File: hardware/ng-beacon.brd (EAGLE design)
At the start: 71.1 x 76.2 mm, 7 parts

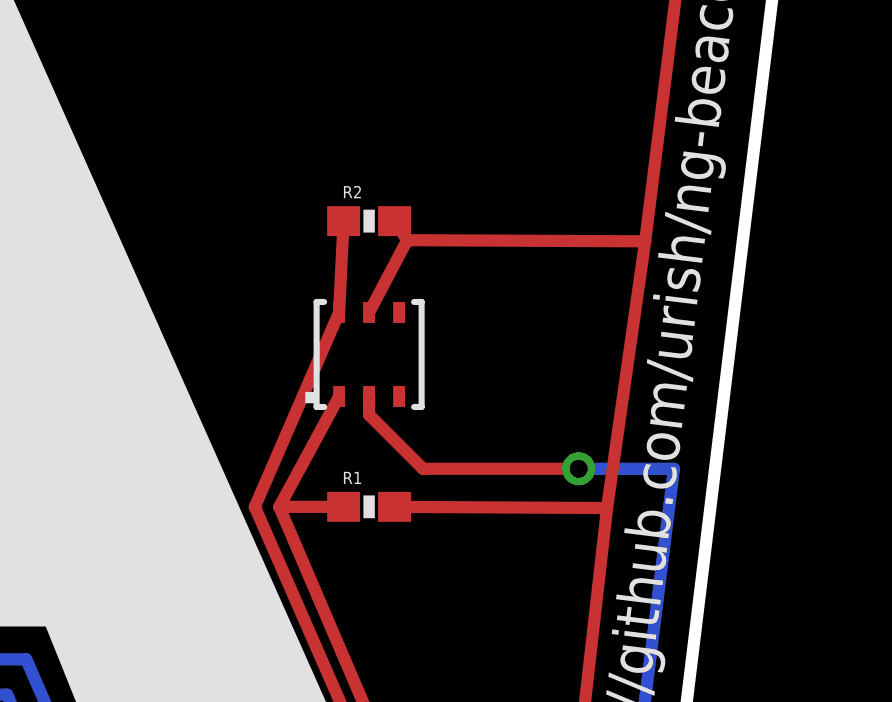
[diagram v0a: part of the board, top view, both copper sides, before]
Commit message: fix(pcb): remove I2C pullup resistors
it works fine without them, as the nRF51 has internal pullups
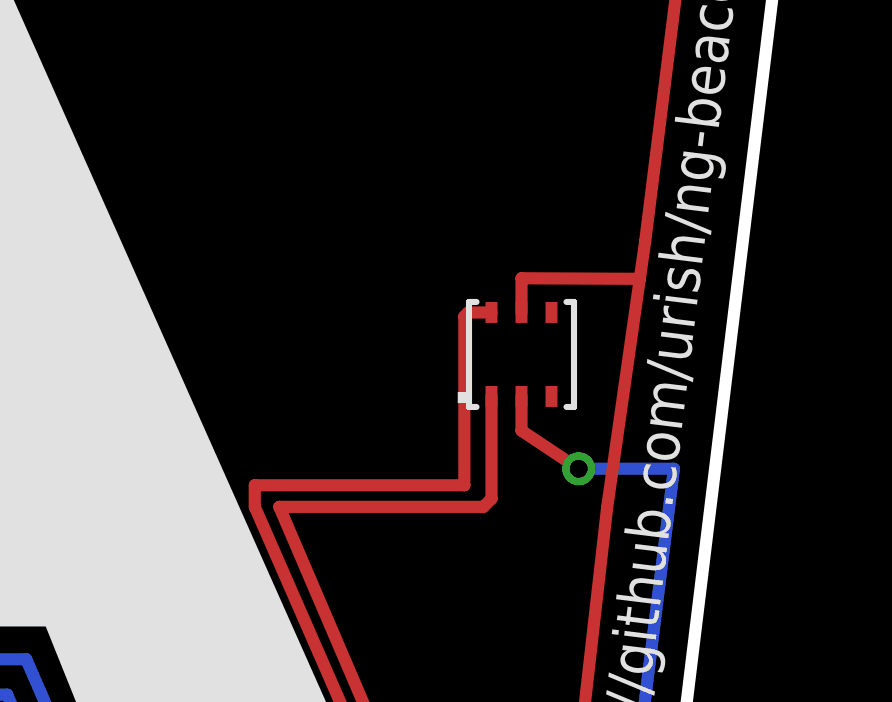
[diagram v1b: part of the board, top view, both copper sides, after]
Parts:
- removed R1, R2: 10K, SparkFun-Resistors:0603-RES
- moved SN1 5.08 mm to (71.1, 35.6)
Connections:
- net SCL: no longer R2.1
- net SDA: no longer R1.1
- net VIN: no longer R1.2, R2.2
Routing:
- net VIN: track 96.9 -> 83.5 mm
- net GND: track 130.4 -> 125.5 mm
- net SDA: track 34.6 -> 38.9 mm
- net SCL: track 35.8 -> 40.0 mm
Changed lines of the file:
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@@
 <attribute name="VALUE" x="64.3222" y="15.616859375" size="1.27" layer="27" rot="R209"/>
 </element>
-<element name="SN1" library="sensirion" package="DFN6/SHT" value="SHT21" x="66.04" y="35.56" smashed="yes">
-<attribute name="VALUE" x="68.915" y="33.685" size="0.8128" layer="27" ratio="10" rot="R90"/>
-</element>
-<element name="R1" library="SparkFun-Resistors" package="0603-RES" value="10K" x="66.04" y="30.48">
-<attribute name="PROD_ID" value="RES-00824" x="66.04" y="30.48" size="1.778" layer="27" display="off"/>
-</element>
-<element name="R2" library="SparkFun-Resistors" package="0603-RES" value="10K" x="66.04" y="40.005">
-<attribute name="PROD_ID" value="RES-00824" x="66.04" y="40.005" size="1.778" layer="27" display="off"/>
+<element name="SN1" library="sensirion" package="DFN6/SHT" value="SHT21" x="71.12" y="35.56" smashed="yes">
+<attribute name="VALUE" x="73.995" y="33.685" size="0.8128" layer="27" ratio="10" rot="R90"/>
 </element>
 </elements>
@@
 <contactref element="SN1" pad="2"/>
 <wire x1="52.07" y1="12.7" x2="58.02453125" y2="8.641059375" width="0.4064" layer="1"/>
-<wire x1="66.04" y1="34.16" x2="66.04" y2="33.54605" width="0.4064" layer="1"/>
-<wire x1="66.04" y1="33.54605" x2="67.83605" y2="31.75" width="0.4064" layer="1"/>
-<wire x1="67.83605" y1="31.75" x2="73.025" y2="31.75" width="0.4064" layer="1"/>
 <via x="73.025" y="31.75" extent="1-16" drill="0.6" shape="square"/>
 <wire x1="73.025" y1="31.75" x2="76.2" y2="31.75" width="0.4064" layer="16"/>
@@
 <wire x1="59.8045" y1="7.40863125" x2="58.600153125" y2="7.71598125" width="0.4064" layer="16"/>
 <wire x1="58.600153125" y1="7.71598125" x2="58.02453125" y2="8.641059375" width="0.4064" layer="16"/>
+<wire x1="73.025" y1="31.75" x2="71.12" y2="33.02" width="0.4064" layer="1"/>
+<wire x1="71.12" y1="33.02" x2="71.12" y2="34.16" width="0.4064" layer="1"/>
 </signal>
 <signal name="N$1">
@@
 <wire x1="69.215" y1="13.97" x2="72.39" y2="16.51" width="0.4064" layer="1"/>
 <wire x1="72.39" y1="16.51" x2="73.972615625" y2="30.440921875" width="0.4064" layer="1"/>
-<wire x1="73.972615625" y1="30.440921875" x2="75.242615625" y2="39.330921875" width="0.4064" layer="1"/>
+<wire x1="73.972615625" y1="30.440921875" x2="75.064034375" y2="38.080853125" width="0.4064" layer="1"/>
+<wire x1="75.064034375" y1="38.080853125" x2="75.242615625" y2="39.330921875" width="0.4064" layer="1"/>
 <wire x1="75.242615625" y1="39.330921875" x2="78.105" y2="62.23" width="0.4064" layer="1"/>
 <wire x1="78.105" y1="62.23" x2="73.9255625" y2="63.7972875" width="0.4064" layer="1"/>
 <wire x1="73.9255625" y1="63.7972875" x2="72.749771875" y2="63.21341875" width="0.4064" layer="1"/>
 <wire x1="72.749771875" y1="63.21341875" x2="72.597159375" y2="62.70240625" width="0.4064" layer="1"/>
-<wire x1="66.04" y1="36.96" x2="67.31" y2="39.37" width="0.4064" layer="1"/>
-<wire x1="67.31" y1="39.37" x2="75.242615625" y2="39.330921875" width="0.4064" layer="1"/>
-<contactref element="R1" pad="2"/>
-<contactref element="R2" pad="2"/>
-<wire x1="66.89" y1="30.48" x2="73.972615625" y2="30.440921875" width="0.4064" layer="1"/>
-<wire x1="66.89" y1="40.005" x2="67.31" y2="39.37" width="0.4064" layer="1"/>
+<wire x1="71.12" y1="36.96" x2="71.12" y2="38.1" width="0.4064" layer="1"/>
+<wire x1="71.12" y1="38.1" x2="75.064034375" y2="38.080853125" width="0.4064" layer="1"/>
 </signal>
 <signal name="SWCLK">
@@
 <contactref element="U$1" pad="14"/>
 <contactref element="SN1" pad="1"/>
-<wire x1="65.04" y1="34.16" x2="63.047734375" y2="30.48" width="0.4064" layer="1"/>
 <wire x1="63.047734375" y1="30.48" x2="67.945" y2="19.05" width="0.4064" layer="1"/>
 <wire x1="67.945" y1="19.05" x2="52.07" y2="19.05" width="0.4064" layer="1"/>
-<contactref element="R1" pad="1"/>
-<wire x1="65.19" y1="30.48" x2="63.047734375" y2="30.48" width="0.4064" layer="1"/>
+<wire x1="63.047734375" y1="30.48" x2="69.85" y2="30.48" width="0.4064" layer="1"/>
+<wire x1="69.85" y1="30.48" x2="70.12" y2="30.75" width="0.4064" layer="1"/>
+<wire x1="70.12" y1="30.75" x2="70.12" y2="34.16" width="0.4064" layer="1"/>
 </signal>
 <signal name="SCL">
 <contactref element="U$1" pad="15"/>
 <contactref element="SN1" pad="6"/>
-<contactref element="R2" pad="1"/>
-<wire x1="65.19" y1="40.005" x2="65.04" y2="36.96" width="0.4064" layer="1"/>
 <wire x1="52.07" y1="20.32" x2="66.675" y2="20.32" width="0.4064" layer="1"/>
 <wire x1="66.675" y1="20.32" x2="62.23" y2="30.48" width="0.4064" layer="1"/>
-<wire x1="62.23" y1="30.48" x2="65.04" y2="36.96" width="0.4064" layer="1"/>
+<wire x1="62.23" y1="30.48" x2="62.23" y2="31.2" width="0.4064" layer="1"/>
+<wire x1="62.23" y1="31.2" x2="69.215" y2="31.2" width="0.4064" layer="1"/>
+<wire x1="69.215" y1="31.2" x2="69.215" y2="36.83" width="0.4064" layer="1"/>
+<wire x1="69.215" y1="36.83" x2="69.345" y2="36.96" width="0.4064" layer="1"/>
+<wire x1="69.345" y1="36.96" x2="70.12" y2="36.96" width="0.4064" layer="1"/>
 </signal>
 <signal name="N$2">

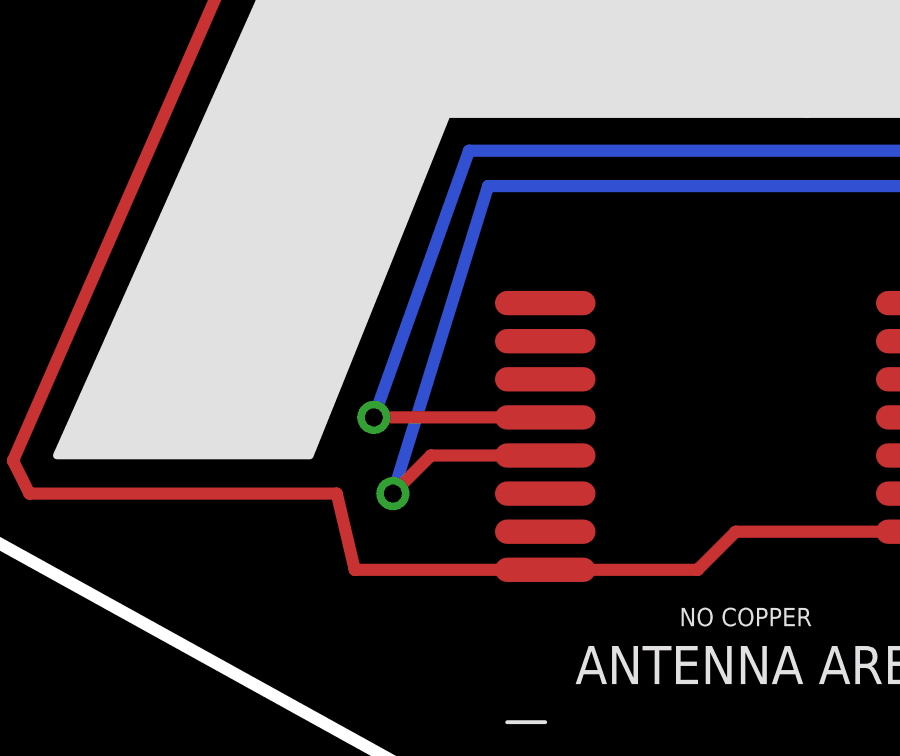
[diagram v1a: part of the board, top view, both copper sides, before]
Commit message: feat: add DFU pads
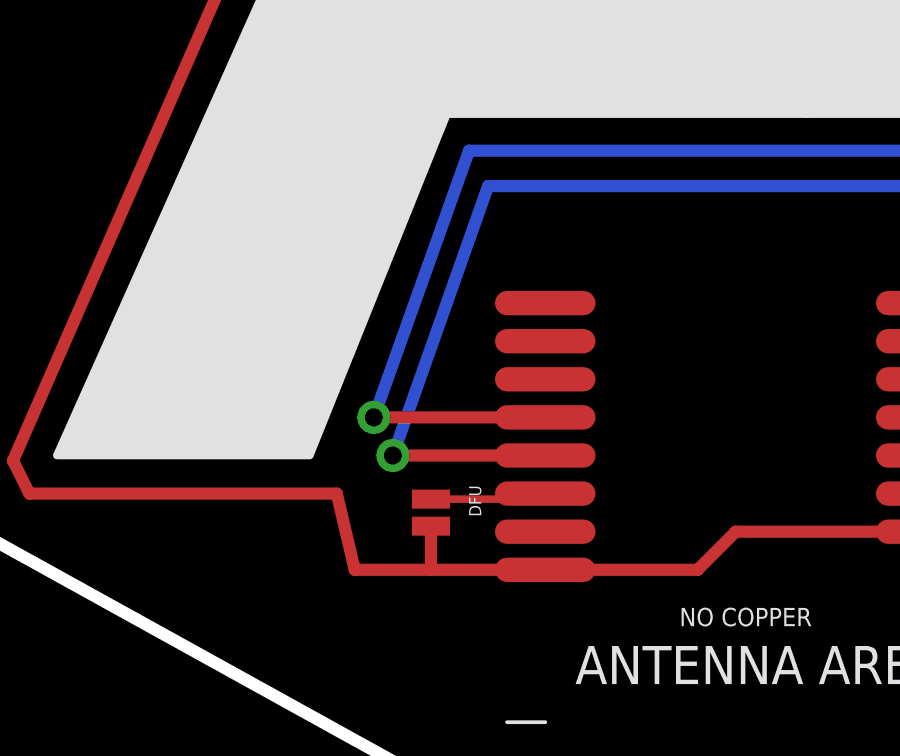
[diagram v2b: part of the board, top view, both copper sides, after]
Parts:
- added DFU: JUMPER-PAD-2-NO, SparkFun-Passives:PAD-JUMPER-2-NO_NO_SILK
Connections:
- new net N$4: DFU.1, U$1.6
- net GND: now also DFU.2
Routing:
- net N$4: track 0.00 -> 3.99 mm
- net SWCLK: track 48.8 -> 47.0 mm
- net GND: track 125.5 -> 127.0 mm
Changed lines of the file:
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@@
 <layer number="220" name="220bmp" color="21" fill="1" visible="no" active="no"/>
 <layer number="221" name="221bmp" color="22" fill="1" visible="no" active="no"/>
+<layer number="222" name="222bmp" color="23" fill="1" visible="no" active="no"/>
 <layer number="223" name="223bmp" color="24" fill="1" visible="no" active="no"/>
 <layer number="224" name="224bmp" color="25" fill="1" visible="no" active="no"/>
@@
 <attribute name="VALUE" x="73.995" y="33.685" size="0.8128" layer="27" ratio="10" rot="R90"/>
 </element>
+<element name="DFU" library="SparkFun-Passives" package="PAD-JUMPER-2-NO_NO_SILK" value="JUMPER-PAD-2-NO" x="35.56" y="13.335" rot="R270"/>
 </elements>
 <signals>
@@
 <wire x1="44.45" y1="11.43" x2="45.72" y2="12.7" width="0.4064" layer="1"/>
 <contactref element="U$1" pad="9"/>
-<wire x1="33.02" y1="11.43" x2="39.37" y2="11.43" width="0.4064" layer="1"/>
+<wire x1="33.02" y1="11.43" x2="35.56" y2="11.43" width="0.4064" layer="1"/>
+<wire x1="35.56" y1="11.43" x2="39.37" y2="11.43" width="0.4064" layer="1"/>
 <wire x1="45.72" y1="12.7" x2="52.07" y2="12.7" width="0.4064" layer="1"/>
 <contactref element="J1" pad="4"/>
@@
 <wire x1="73.025" y1="31.75" x2="71.12" y2="33.02" width="0.4064" layer="1"/>
 <wire x1="71.12" y1="33.02" x2="71.12" y2="34.16" width="0.4064" layer="1"/>
+<contactref element="DFU" pad="2"/>
+<wire x1="35.56" y1="12.885" x2="35.56" y2="11.43" width="0.4064" layer="1"/>
 </signal>
 <signal name="N$1">
@@
 <wire x1="59.69" y1="10.795" x2="53.975" y2="24.22" width="0.4064" layer="16"/>
 <wire x1="53.975" y1="24.22" x2="37.465" y2="24.22" width="0.4064" layer="16"/>
-<wire x1="37.465" y1="24.22" x2="34.29" y2="13.97" width="0.4064" layer="16"/>
-<via x="34.29" y="13.97" extent="1-16" drill="0.6" shape="square"/>
-<wire x1="39.37" y1="15.24" x2="35.56" y2="15.24" width="0.4064" layer="1"/>
-<wire x1="35.56" y1="15.24" x2="34.29" y2="13.97" width="0.4064" layer="1"/>
+<wire x1="37.465" y1="24.22" x2="34.29" y2="15.24" width="0.4064" layer="16"/>
+<via x="34.29" y="15.24" extent="1-16" drill="0.6" shape="square"/>
+<wire x1="39.37" y1="15.24" x2="34.29" y2="15.24" width="0.4064" layer="1"/>
 </signal>
 <signal name="SWDIO">
@@
 <signal name="N$2">
 </signal>
+<signal name="N$4">
+<contactref element="U$1" pad="6"/>
+<contactref element="DFU" pad="1"/>
+<wire x1="35.56" y1="13.785" x2="39.37" y2="13.785" width="0.254" layer="1"/>
+<wire x1="39.37" y1="13.785" x2="39.37" y2="13.97" width="0.254" layer="1"/>
+</signal>
 </signals>

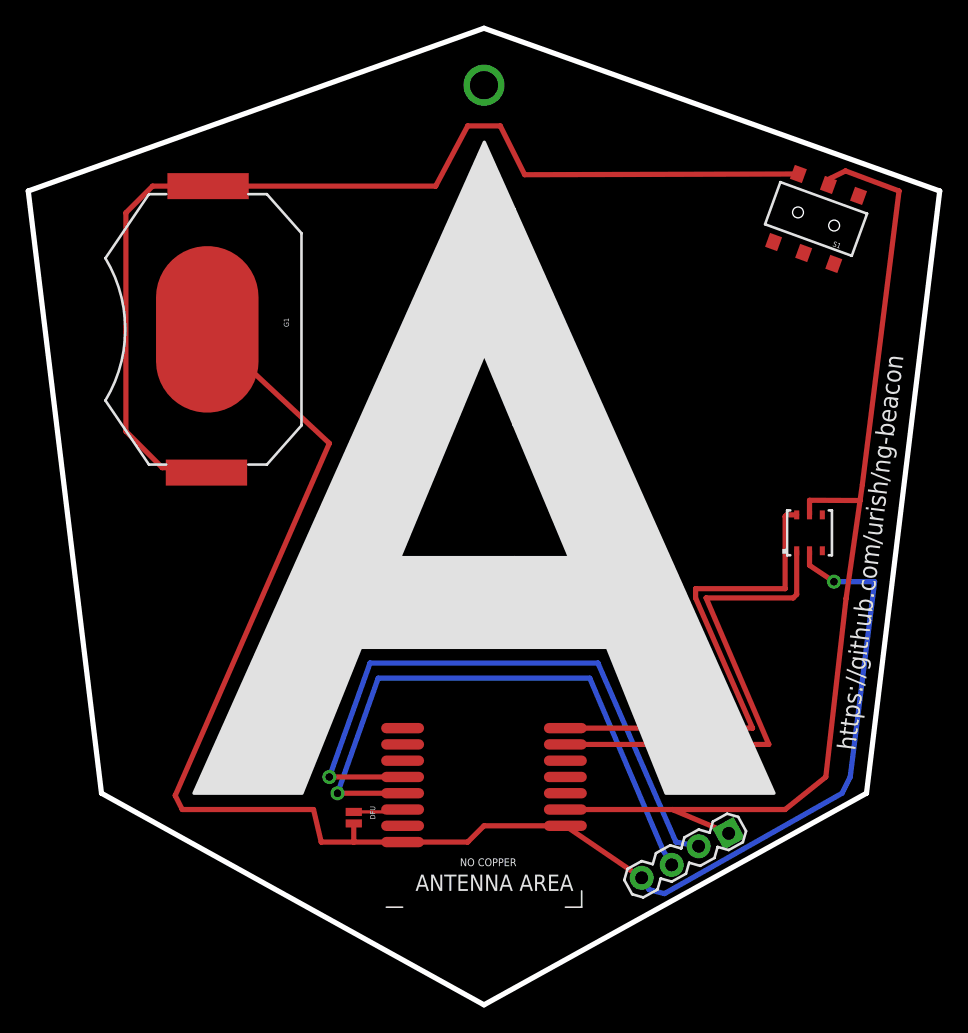
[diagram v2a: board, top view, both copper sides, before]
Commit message: fix: update board layout for PTR5618
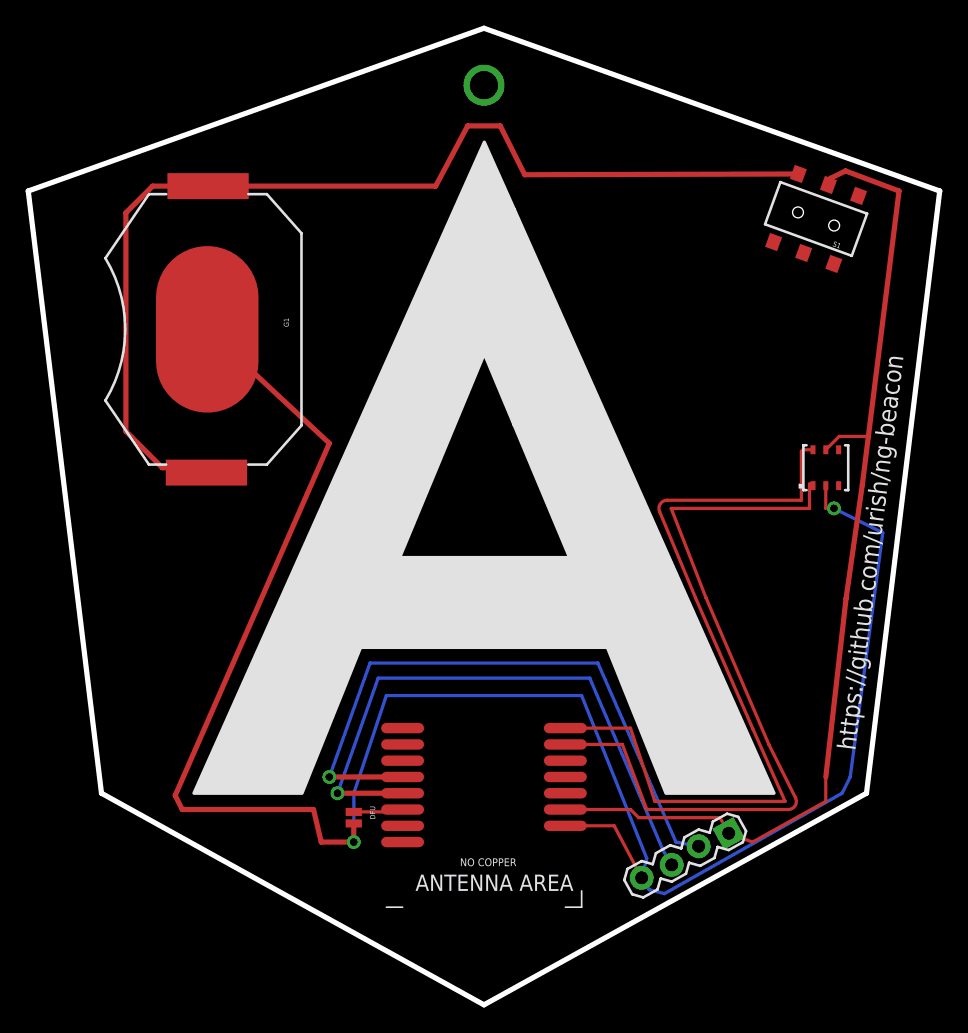
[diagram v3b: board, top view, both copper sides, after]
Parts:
- moved SN1 5.24 mm to (72.4, 40.6)
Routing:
- net GND: track 127.0 -> 157.4 mm, vias 1 -> 2
- net SCL: track 40.0 -> 62.2 mm
- net SDA: track 38.9 -> 59.6 mm
- net N$1: track 86.9 -> 91.0 mm
- net VIN: track 83.5 -> 80.3 mm

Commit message: Add a prototype area with PO.26, 27, SDA, and SCL.
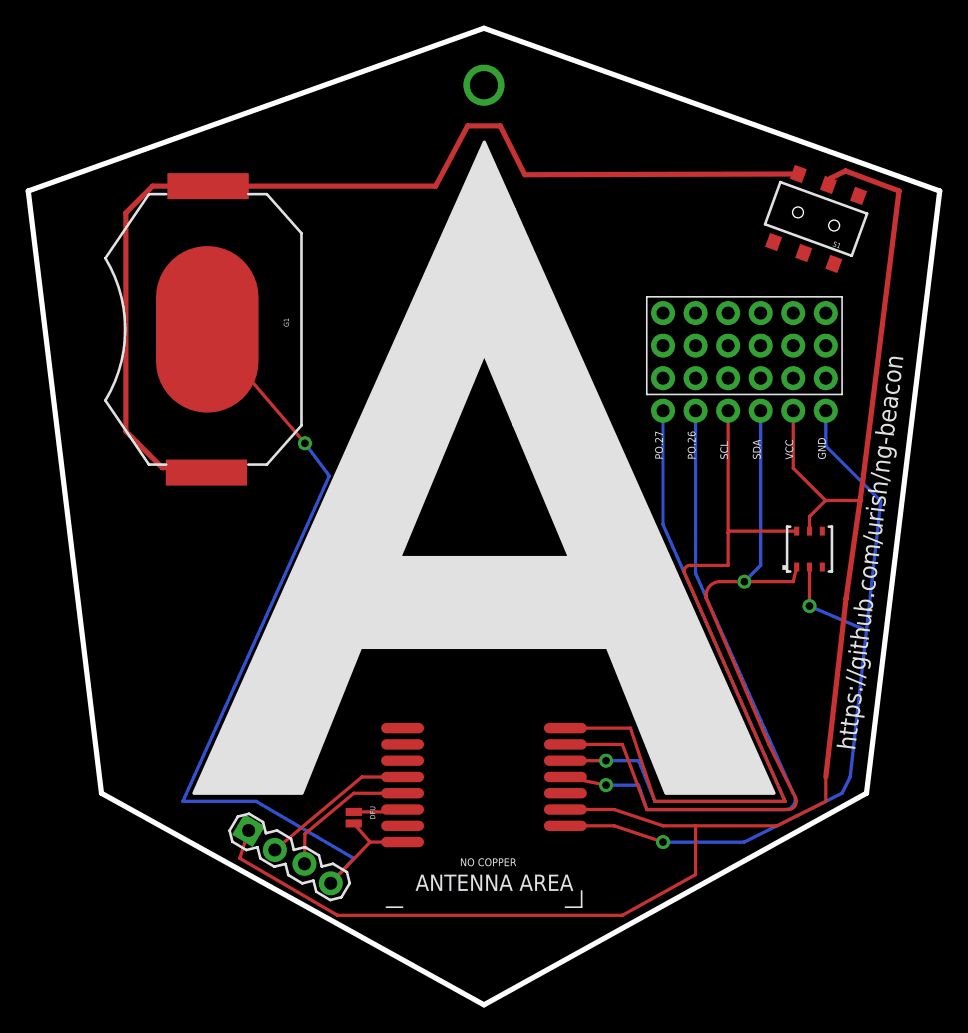
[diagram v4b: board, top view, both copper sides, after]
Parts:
- added J3: (no value), heathkit:PROTO4X6
- moved J1 37.5 mm to (27.3, 12.2), turned to 329.2 degrees
- moved SN1 6.48 mm to (71.1, 34.3)
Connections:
- new net N$5: J3.P$2, U$1.12
- new net N$6: J3.P$1, U$1.13
- net GND: now also J3.P$6
- net SCL: now also J3.P$3
- net SDA: now also J3.P$4
- net VIN: now also J3.P$5
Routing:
- net VIN: track 80.3 -> 132.6 mm
- net N$6: track 0.00 -> 51.8 mm, vias 0 -> 1
- net N$5: track 0.00 -> 51.5 mm, vias 0 -> 1
- net SWDIO: track 50.0 -> 12.0 mm, vias 1 -> 0
- net SWCLK: track 47.0 -> 11.1 mm, vias 1 -> 0
- net GND: track 157.4 -> 131.3 mm, vias 2 -> 3
- net SDA: track 59.6 -> 61.5 mm, vias 0 -> 1
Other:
- board text added: "GND"
- board text added: "PO.26"
- board text added: "PO.27"
- board text added: "SCL"
- board text added: "SDA"
- board text added: "VCC"
